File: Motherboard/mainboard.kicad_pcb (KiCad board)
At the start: 4 copper layers, 45.2 x 36 mm, 53 parts, among them IC1 BMX160, J1 Conn_01x01, J2 10118194-0001LF, J28 Conn_01x01, J29 Conn_01x01, J3 Micro_SD_Card, J30 Conn_01x01, J4 xf2m-2415-1a, J5 XF2M-1015-1A, J6 U.FL-R-SMT-1, J7 U.FL-R-SMT-1, J8 Conn_01x01, J9 XF2M36151A, SW1 KMR231NG LFS, U1 RFM95W-915S2, U2 ATSAMD51G_TQFN48, U3 DRV8848, U4 TPS82740BSIPR, U5 DRV8848, U6 MAX708RESA-T, U8 RFM95W-915S2

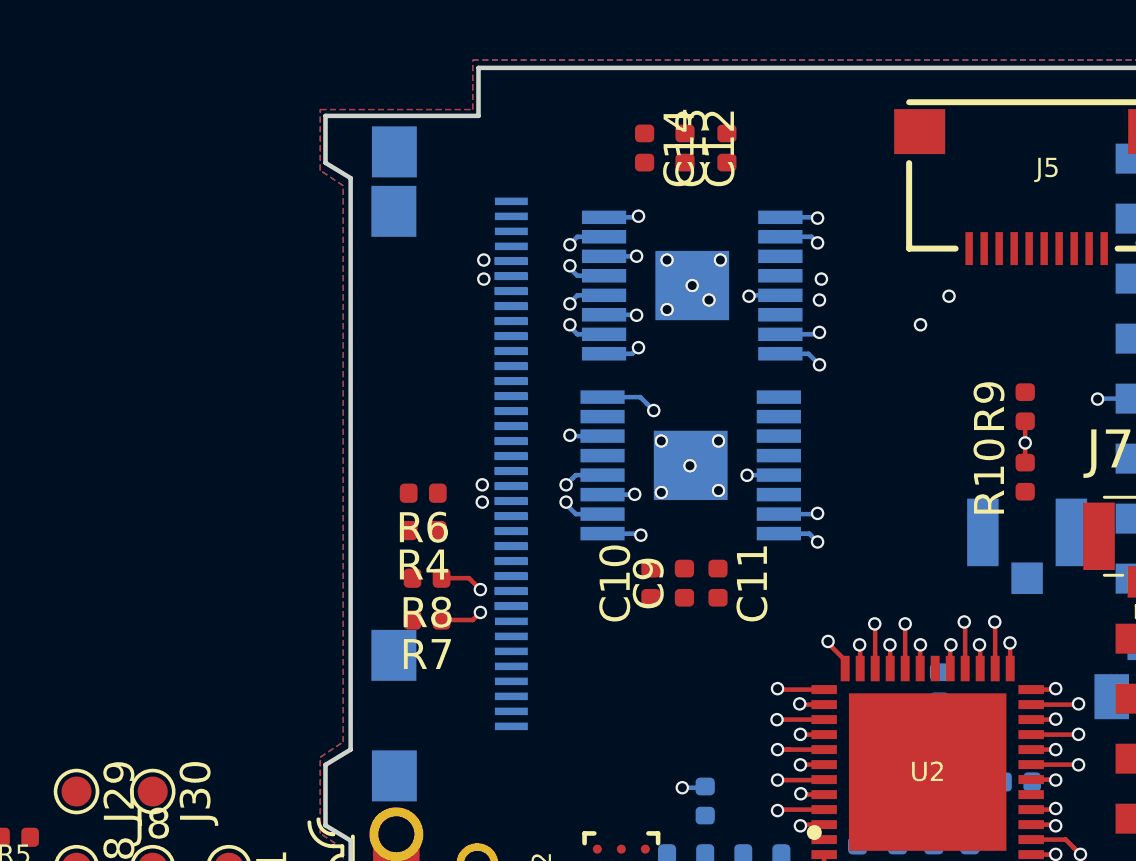
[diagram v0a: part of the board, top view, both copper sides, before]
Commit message: coil bridges with contingency finished
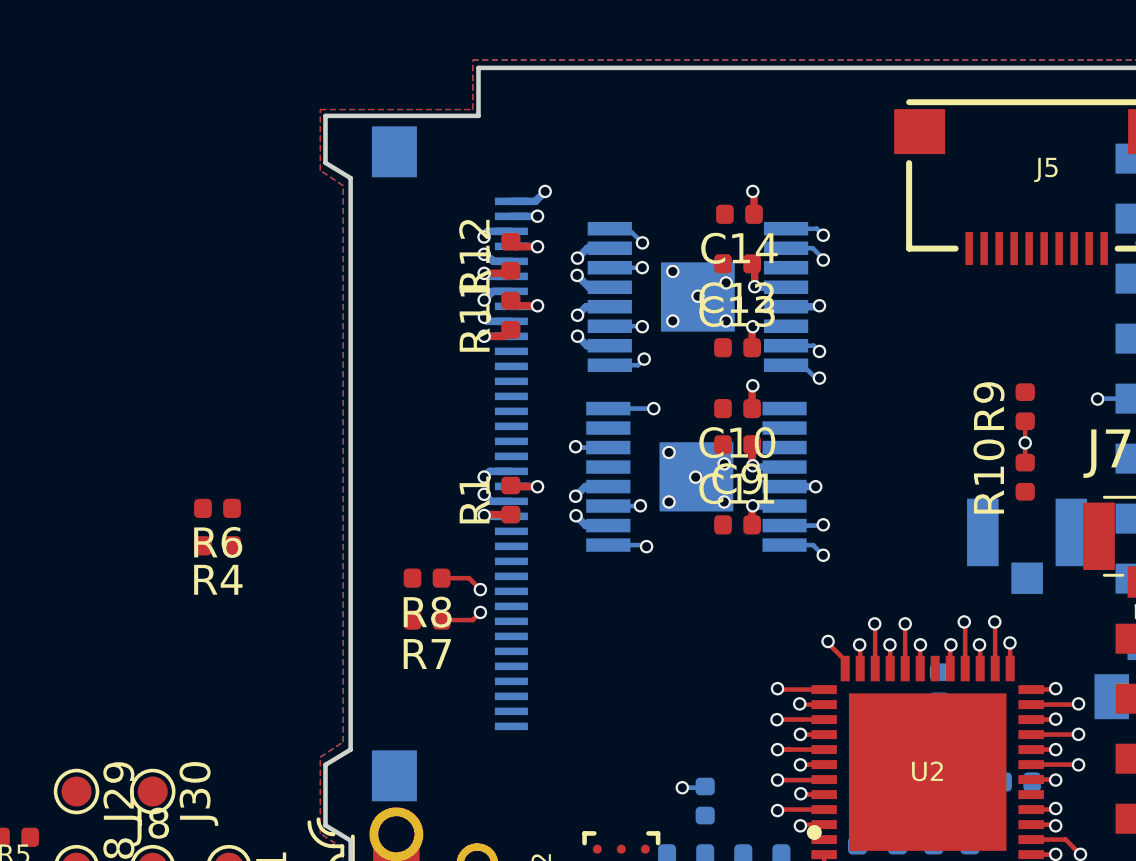
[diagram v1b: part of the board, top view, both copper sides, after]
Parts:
- removed J4: xf2m-2415-1a, custom-footprints:XF2M-2415-1A
- added R1: 0, Resistor_SMD:R_0402_1005Metric, F.Cu at (82.8, 87.9)
- added R11: 0, Resistor_SMD:R_0402_1005Metric, F.Cu at (82.8, 81.8)
- added R12: 0, Resistor_SMD:R_0402_1005Metric, F.Cu at (82.8, 79.8)
- moved R4 6.88 mm to (73.0, 89.5)
- moved R6 6.88 mm to (73.0, 88.2)
- moved C13 6.66 mm to (90.4, 82.9), turned to 0 degrees
- moved C10 6.50 mm to (90.4, 84.9), turned to 180 degrees
- moved C9 4.94 mm to (90.4, 86.1), turned to 180 degrees
- moved C12 4.24 mm to (90.4, 80.1), turned to 180 degrees
- moved C14 3.86 mm to (90.4, 78.4), turned to 180 degrees
- moved C11 2.05 mm to (90.4, 88.8), turned to 0 degrees
- moved U3 0.43 mm to (89.0, 81.2)
- moved U5 0.43 mm to (89.0, 87.2)
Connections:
- net Net-(J9-Pad16) renamed COIL6_N
- net Net-(J9-Pad18) renamed COIL5_P
- net Net-(J9-Pad28) renamed COIL4_N
- net Net-(J9-Pad30) renamed COIL3_P
- net Net-(J9-Pad32) renamed COIL2_N
- net Net-(J9-Pad34) renamed COIL1_P
- C11 pad 2: 3V3 -> +3V3
- C13 pad 2: 3V3 -> +3V3
- J9 pad 35: Net-(J9-Pad35) -> GND
- J9 pad 36: Net-(J9-Pad36) -> BATT_P
- U3 pad 11: 3V3 -> +3V3
- U3 pad 14: 3V3 -> +3V3
- U5 pad 11: 3V3 -> +3V3
- U5 pad 14: 3V3 -> +3V3
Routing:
- net BATT_P: track 0.00 -> 30.7 mm, vias 0 -> 5
- net (no net): track 30.2 -> 0.00 mm, vias 4 -> 0
- net MOX_1: track 4.55 -> 1.21 mm
- net MOX_2: track 4.49 -> 1.19 mm
- net MOY_1: track 4.45 -> 1.21 mm, vias 2 -> 1
- net MOZ_2: track 4.49 -> 1.25 mm, vias 2 -> 1
- net MOZ_1: track 4.34 -> 1.21 mm, vias 2 -> 1
- net MOY_2: track 4.25 -> 1.22 mm, vias 2 -> 1
- net MISO: track 59.1 -> 56.5 mm
- net +3V3: track 6.71 -> 9.25 mm, vias 8 -> 10
- net Net-(J9-Pad27): track 0.00 -> 1.89 mm, vias 0 -> 1
- net Net-(J9-Pad31): track 0.00 -> 1.87 mm, vias 0 -> 1
- net Net-(J9-Pad29): track 0.00 -> 1.84 mm, vias 0 -> 1
- net Net-(J9-Pad33): track 0.00 -> 1.83 mm, vias 0 -> 1
- net Net-(J9-Pad15): track 0.00 -> 1.82 mm, vias 0 -> 1
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
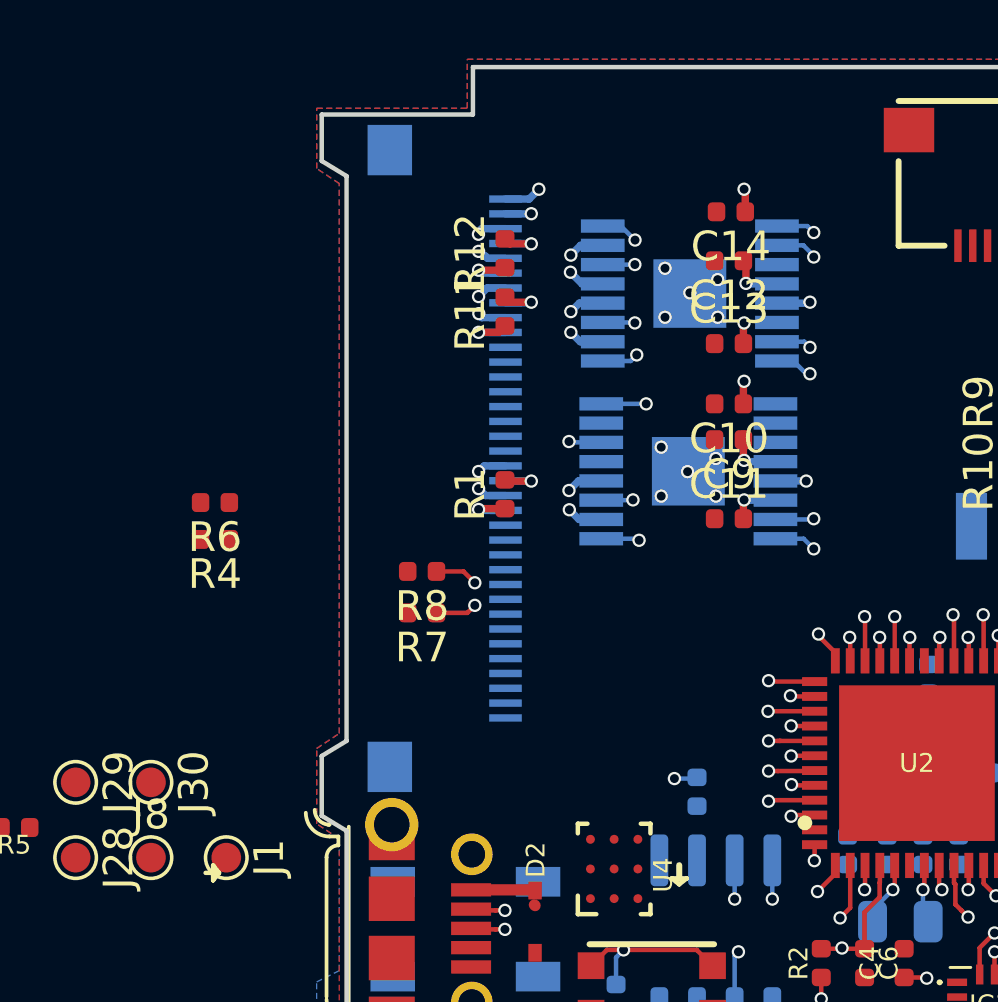
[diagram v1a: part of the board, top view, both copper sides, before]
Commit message: big FPC routed
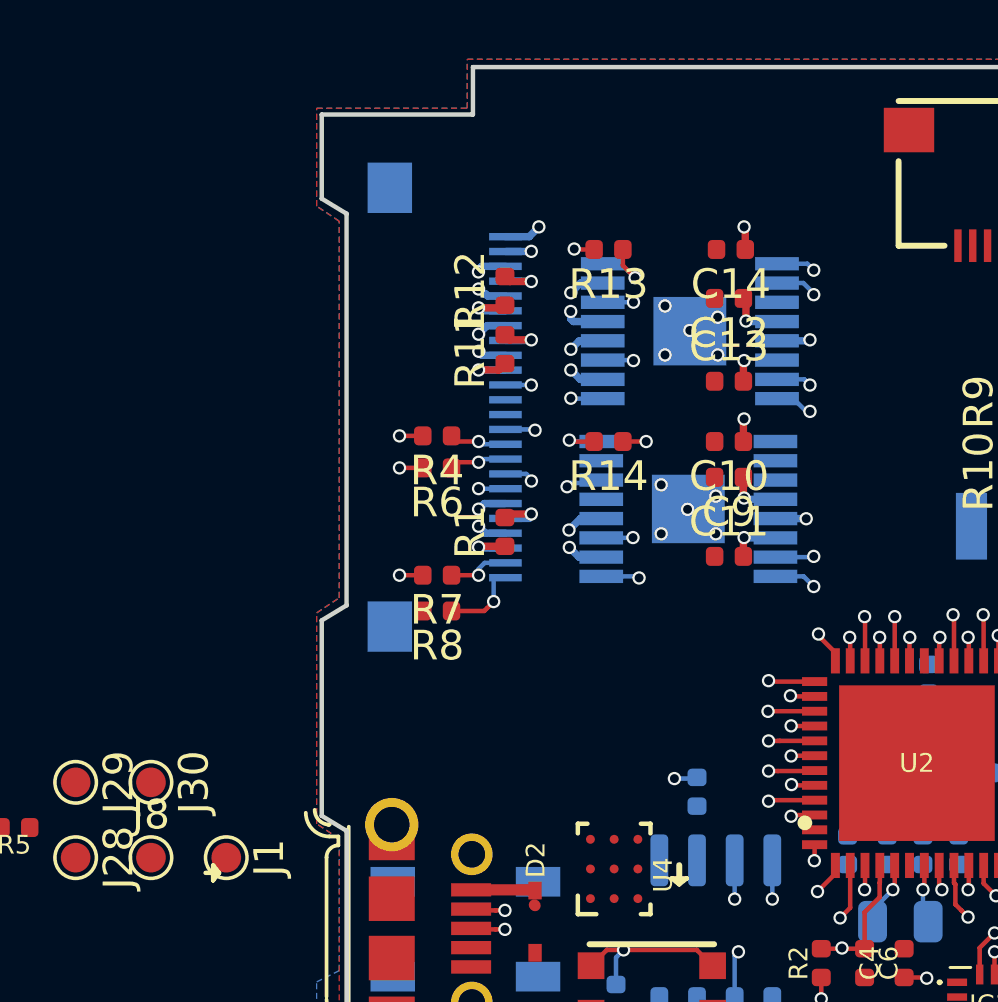
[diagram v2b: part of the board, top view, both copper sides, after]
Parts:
- removed J9: XF2M36151A, custom-footprints:XF2M36151A
- added J4: xf2m-2415-1a, custom-footprints:XF2M-2415-1A, B.Cu at (82.8, 85.0)
- added R13: 100K, Resistor_SMD:R_0402_1005Metric, F.Cu at (86.3, 79.7)
- added R14: 10K, Resistor_SMD:R_0402_1005Metric, F.Cu at (86.3, 86.2)
- moved R4 8.27 mm to (80.5, 86.0)
- moved R6 7.58 mm to (80.5, 87.1)
- moved R8 1.43 mm to (80.5, 91.9)
- moved R7 1.37 mm to (80.5, 90.7)
- moved C11 1.27 mm to (90.4, 90.0)
- moved C12 1.27 mm to (90.4, 81.3)
- moved C9 1.27 mm to (90.4, 87.4)
- moved R11 1.27 mm to (82.8, 83.1)
- moved U3 1.27 mm to (89.0, 82.4)
- moved U5 1.27 mm to (89.0, 88.4)
- moved C10 1.27 mm to (90.4, 86.2)
- moved C13 1.27 mm to (90.4, 84.1)
- moved C14 1.27 mm to (90.4, 79.7)
- moved R1 1.27 mm to (82.8, 89.2)
- moved R12 1.27 mm to (82.8, 81.1)
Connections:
- U3 pad 2: MOX_1 -> COIL4_N
- U3 pad 4: MOX_2 -> COIL3_P
- U3 pad 5: MOZ_2 -> COIL2_N
- U3 pad 7: MOZ_1 -> COIL1_P
- U5 pad 2: MOY_1 -> COIL6_N
- U5 pad 4: MOY_2 -> COIL5_P
- U5 pad 8: M_FAULT -> M_FAULT2
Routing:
- net SCL1: track 29.3 -> 34.9 mm, vias 2 -> 3
- net SDA1: track 27.2 -> 32.6 mm, vias 2 -> 3
- net COIL2_N: track 1.00 -> 5.79 mm, vias 1 -> 2
- net COIL1_P: track 1.03 -> 5.81 mm, vias 1 -> 2
- net COIL5_P: track 0.99 -> 5.73 mm, vias 1 -> 2
- net COIL3_P: track 1.03 -> 5.73 mm, vias 1 -> 2
- net COIL4_N: track 0.97 -> 5.55 mm, vias 1 -> 2
- net COIL6_N: track 1.00 -> 5.57 mm, vias 1 -> 2
- net BURN1: track 13.1 -> 17.1 mm, vias 1 -> 2
- net BATT_STATUS: track 12.8 -> 16.7 mm, vias 1 -> 2
- net BURN2: track 12.9 -> 16.4 mm, vias 1 -> 2
- net +3V3: track 9.25 -> 12.3 mm, vias 10 -> 14
- net M_FAULT2: track 0.00 -> 1.95 mm, vias 0 -> 1
- net SDA2: track 14.1 -> 15.8 mm
- net MINX_2: track 12.5 -> 11.3 mm
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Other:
- outline, holes or cut-outs redrawn

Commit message: neopixel 🚥
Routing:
- net RF2_BUSY: track 14.0 -> 11.5 mm
- net Net-(D3-Pad4): track 10.2 -> 11.8 mm, vias 1 -> 2
- net GND: track 11.7 -> 12.7 mm, vias 21 -> 22
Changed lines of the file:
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@@
     (thickness 1.2)
     (drawings 38)
-    (tracks 678)
+    (tracks 681)
     (zones 0)
     (modules 57)
@@
   )
   (setup
-    (last_trace_width 0.1524)
+    (last_trace_width 0.25)
     (user_trace_width 0.1524)
     (user_trace_width 0.25)
@@
   (segment (start 86.0509 87.4678) (end 85.9522 87.5665) (width 0.1524) (layer Bottom) (net 1))
   (segment (start 85.9522 87.5665) (end 85.026496 87.5665) (width 0.1524) (layer Bottom) (net 1))
+  (via (at 83.947 100.0125) (size 0.45) (drill 0.3) (layers Top Bottom) (net 1))
+  (segment (start 83.9205 101.016) (end 83.9205 100.039) (width 0.25) (layer Bottom) (net 1))
+  (segment (start 83.9205 100.039) (end 83.947 100.0125) (width 0.25) (layer Bottom) (net 1))
   (via (at 92.45601 98.806) (size 0.45) (drill 0.3) (layers Top Bottom) (net 2))
   (segment (start 93.2478 98.7653) (end 92.49671 98.7653) (width 0.1524) (layer Top) (net 2))
@@
   (segment (start 99.36375 101.489357) (end 99.697607 101.1555) (width 0.1524) (layer In1.Cu) (net 24))
   (segment (start 99.697607 101.1555) (end 114.173 101.1555) (width 0.1524) (layer In1.Cu) (net 24))
-  (via (at 105.3465 98.552) (size 0.45) (drill 0.3) (layers Top Bottom) (net 29))
-  (segment (start 103.86 98.568) (end 105.3305 98.568) (width 0.1524) (layer Top) (net 29))
-  (segment (start 105.3305 98.568) (end 105.3465 98.552) (width 0.1524) (layer Top) (net 29))
   (via (at 94.9325 101.2825) (size 0.45) (drill 0.3) (layers Top Bottom) (net 29))
   (segment (start 94.9478 100.4653) (end 94.9478 101.2672) (width 0.1524) (layer Top) (net 29))
   (segment (start 94.9478 101.2672) (end 94.9325 101.2825) (width 0.1524) (layer Top) (net 29))
-  (segment (start 104.013 98.552) (end 105.3465 98.552) (width 0.1524) (layer In1.Cu) (net 29))
-  (segment (start 98.7425 100.711) (end 99.314 100.1395) (width 0.1524) (layer In1.Cu) (net 29))
-  (segment (start 95.504 100.711) (end 98.7425 100.711) (width 0.1524) (layer In1.Cu) (net 29))
-  (segment (start 99.314 100.1395) (end 100.584 100.1395) (width 0.1524) (layer In1.Cu) (net 29))
-  (segment (start 102.235 100.33) (end 104.013 98.552) (width 0.1524) (layer In1.Cu) (net 29))
-  (segment (start 94.9325 101.2825) (end 95.504 100.711) (width 0.1524) (layer In1.Cu) (net 29))
-  (segment (start 100.584 100.1395) (end 100.7745 100.33) (width 0.1524) (layer In1.Cu) (net 29))
-  (segment (start 100.7745 100.33) (end 102.235 100.33) (width 0.1524) (layer In1.Cu) (net 29))
   (via (at 101.727008 96.774) (size 0.45) (drill 0.3) (layers Top Bottom) (net 31))
   (segment (start 101.718308 96.7653) (end 101.727008 96.774) (width 0.1524) (layer Top) (net 31))
@@
   (segment (start 119.66 96.568) (end 118.189 96.568) (width 0.1524) (layer Top) (net 31))
   (segment (start 118.189 96.568) (end 118.1735 96.5835) (width 0.1524) (layer Top) (net 31))
-  (segment (start 102.9208 96.774) (end 101.727008 96.774) (width 0.1524) (layer In1.Cu) (net 31))
-  (segment (start 118.1735 96.5835) (end 103.1113 96.5835) (width 0.1524) (layer In1.Cu) (net 31))
-  (segment (start 103.1113 96.5835) (end 102.9208 96.774) (width 0.1524) (layer In1.Cu) (net 31))
   (segment (start 88.011 105.445) (end 89.281 105.445) (width 0.1524) (layer Bottom) (net 32))
   (segment (start 88.0055 105.4505) (end 88.011 105.445) (width 0.1524) (layer Bottom) (net 32))
@@
   (segment (start 119.66 86.566) (end 119.66 87.4135) (width 0.1524) (layer Bottom) (net 69))
   (segment (start 119.66 87.4135) (end 119.634 87.4395) (width 0.1524) (layer Bottom) (net 69))
-  (segment (start 103.124 96.266) (end 100.965 96.266) (width 0.1524) (layer In1.Cu) (net 69))
-  (segment (start 103.55834 95.83166) (end 103.124 96.266) (width 0.1524) (layer In1.Cu) (net 69))
-  (segment (start 119.634 87.4395) (end 111.24184 95.83166) (width 0.1524) (layer In1.Cu) (net 69))
-  (segment (start 111.24184 95.83166) (end 103.55834 95.83166) (width 0.1524) (layer In1.Cu) (net 69))
   (via (at 101.727 95.758) (size 0.45) (drill 0.3) (layers Top Bottom) (net 70))
   (segment (start 100.1478 95.7653) (end 101.7197 95.7653) (width 0.1524) (layer Top) (net 70))
@@
   (segment (start 93.345 101.3431) (end 93.345 101.34601) (width 0.1524) (layer Top) (net 77))
   (segment (start 93.9478 100.4653) (end 93.9478 100.7403) (width 0.1524) (layer Top) (net 77))
-  (segment (start 92.2655 102.4255) (end 84.7725 102.4255) (width 0.1524) (layer In1.Cu) (net 77))
-  (segment (start 93.345 101.34601) (end 93.34499 101.34601) (width 0.1524) (layer In1.Cu) (net 77))
-  (segment (start 93.34499 101.34601) (end 92.2655 102.4255) (width 0.1524) (layer In1.Cu) (net 77))
   (via (at 83.693 80.772) (size 0.45) (drill 0.3) (layers Top Bottom) (net 86))
   (segment (start 82.822 80.761) (end 83.682 80.761) (width 0.25) (layer Bottom) (net 86))
@@
   (segment (start 82.9715 82.7405) (end 82.804 82.573) (width 0.25) (layer Top) (net 26))
   (segment (start 83.693 82.7405) (end 82.9715 82.7405) (width 0.25) (layer Top) (net 26))
+  (via (at 103.886 99.377496) (size 0.45) (drill 0.3) (layers Top Bottom) (net 29))
+  (segment (start 102.933496 100.33) (end 103.661001 99.602495) (width 0.1524) (layer In1.Cu) (net 29))
+  (segment (start 103.86 98.568) (end 103.86 99.351496) (width 0.1524) (layer Top) (net 29))
+  (segment (start 100.7745 100.33) (end 102.933496 100.33) (width 0.1524) (layer In1.Cu) (net 29))
+  (segment (start 103.661001 99.602495) (end 103.886 99.377496) (width 0.1524) (layer In1.Cu) (net 29))
+  (segment (start 100.584 100.1395) (end 100.7745 100.33) (width 0.1524) (layer In1.Cu) (net 29))
+  (segment (start 96.0755 100.1395) (end 100.584 100.1395) (width 0.1524) (layer In1.Cu) (net 29))
+  (segment (start 94.9325 101.2825) (end 96.0755 100.1395) (width 0.1524) (layer In1.Cu) (net 29))
+  (segment (start 103.86 99.351496) (end 103.886 99.377496) (width 0.1524) (layer Top) (net 29))
+  (segment (start 102.9208 96.774) (end 101.727008 96.774) (width 0.1524) (layer In1.Cu) (net 31))
+  (segment (start 118.1735 96.5835) (end 117.983 96.774) (width 0.1524) (layer In1.Cu) (net 31))
+  (segment (start 117.983 96.774) (end 102.9208 96.774) (width 0.1524) (layer In1.Cu) (net 31))
   (via (at 81.915 90.678) (size 0.45) (drill 0.3) (layers Top Bottom) (net 39))
   (segment (start 82.82178 90.26126) (end 82.11938 90.26126) (width 0.1524) (layer Bottom) (net 39))
@@
   (segment (start 82.92301 88.61349) (end 83.693 88.61349) (width 0.25) (layer Top) (net 51))
   (segment (start 82.804 88.7325) (end 82.92301 88.61349) (width 0.25) (layer Top) (net 51))
+  (segment (start 110.8075 96.266) (end 100.965 96.266) (width 0.1524) (layer In1.Cu) (net 69))
+  (segment (start 119.634 87.4395) (end 110.8075 96.266) (width 0.1524) (layer In1.Cu) (net 69))
   (via (at 83.82 85.7885) (size 0.45) (drill 0.3) (layers Top Bottom) (net 72))
   (segment (start 82.82178 85.76126) (end 83.79276 85.76126) (width 0.1524) (layer Bottom) (net 72))
@@
   (segment (start 85.513609 88.955309) (end 85.513609 85.196105) (width 0.1524) (layer In2.Cu) (net 74))
   (segment (start 85.513609 85.196105) (end 85.251503 84.933999) (width 0.1524) (layer In2.Cu) (net 74))
+  (via (at 84.6455 103.378) (size 0.45) (drill 0.3) (layers Top Bottom) (net 77))
+  (segment (start 83.9205 104.216) (end 83.9205 104.103) (width 0.1524) (layer Bottom) (net 77))
+  (segment (start 83.9205 104.103) (end 84.6455 103.378) (width 0.1524) (layer Bottom) (net 77))
+  (segment (start 85.598 102.4255) (end 84.6455 103.378) (width 0.1524) (layer In1.Cu) (net 77))
+  (segment (start 92.2655 102.4255) (end 85.598 102.4255) (width 0.1524) (layer In1.Cu) (net 77))
+  (segment (start 93.345 101.34601) (end 93.34499 101.34601) (width 0.1524) (layer In1.Cu) (net 77))
+  (segment (start 93.34499 101.34601) (end 92.2655 102.4255) (width 0.1524) (layer In1.Cu) (net 77))
   (segment (start 81.944987 89.761) (end 81.915 89.731013) (width 0.25) (layer Bottom) (net 78))
   (segment (start 82.822 89.761) (end 81.944987 89.761) (width 0.25) (layer Bottom) (net 78))

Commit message: 100% routed
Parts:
- removed J28, J29, J30, J8: Conn_01x01, TestPoint:TestPoint_Pad_D1.0mm
- added J9: Conn_01x02, Connector_PinHeader_2.54mm:PinHeader_1x02_P2.54mm_Vertical, F.Cu at (90.0, 77.0)
- J1: value Conn_01x01 -> Conn_01x06; footprint TestPoint:TestPoint_Pad_D1.0mm -> Connector_PinHeader_1.27mm:PinHeader_2x03_P1.27mm_Vertical_SMD
- moved R5 22.2 mm to (88.1, 95.4), turned to 180 degrees
- moved J1 10.6 mm to (82.9, 95.4), turned to 0 degrees
- moved J5 1.49 mm to (99.8, 81.0)
- moved C16 0.63 mm to (88.8, 98.4), turned to 180 degrees
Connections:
- J1 pad 1: /SWDIO -> +3V3
- J3 pad SH1: (no net) -> GND
- J5 pad 4: BATT_N -> GND
- J5 pad 5: EN_CAM -> MOSI
- J5 pad 6: CS_CAM -> SCK
- J5 pad 8: MOSI -> EN_CAM
- J5 pad 9: SCK -> CS_CAM
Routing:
- net BATT_P: track 30.7 -> 44.9 mm, vias 5 -> 7
- net /SWCLK: track 7.63 -> 20.0 mm, vias 1 -> 2
- net /SWDIO: track 6.02 -> 17.7 mm, vias 1 -> 2
- net ~RESET: track 18.4 -> 28.5 mm, vias 2 -> 3
- net MISO: track 56.5 -> 66.5 mm, vias 4 -> 5
- net /USB+: track 4.56 -> 12.9 mm
- net /USB-: track 5.13 -> 13.3 mm
- net CS_CAM: track 10.4 -> 15.5 mm, vias 1 -> 2
- net GND: track 12.7 -> 16.1 mm, vias 22 -> 24
- net EN_CAM: track 10.5 -> 12.9 mm, vias 1 -> 2
- net MOSI: track 57.1 -> 58.9 mm, vias 4 -> 5
- net +3V3: track 12.3 -> 13.9 mm, vias 14 -> 15
- net SCK: track 55.1 -> 55.5 mm, vias 4 -> 5

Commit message: finished- might fiddle with later
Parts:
- moved D2 2.03 mm to (83.8, 100.3), turned to 270 degrees
- moved R5 1.88 mm to (87.2, 97.1), turned to 90 degrees
- renumbered IC1 to U7
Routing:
- net GND: track 16.1 -> 29.9 mm, vias 24 -> 38
- net Net-(D2-Pad1): track 0.00 -> 5.59 mm
- net +3V3: track 13.9 -> 18.5 mm, vias 15 -> 21
- net Net-(J6-Pad3): track 0.00 -> 3.85 mm
- net Net-(J7-Pad3): track 0.00 -> 1.86 mm
- net ~RESET: track 28.5 -> 29.9 mm
- net MINY_2: track 11.9 -> 10.6 mm
- net MINY_1: track 5.51 -> 4.24 mm
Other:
- board text added: "BATTP"
- board text added: "RADIO #1"
- board text added: "RADIO #2"
- board text added: "RST"
- board text added: "~RESET"

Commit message: fab files for max version of MB
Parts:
- added Ref**: Val**, custom-footprints:XYZ_mini, F.Cu at (110.0, 81.3)
- added Ref**: Val**, custom-footprints:holliday, B.Cu at (76.3, 94.8)
- added Ref**: Val**, custom-footprints:version, B.Cu at (93.9, 105.6)
- added Ref**: Val**, custom-footprints:version, F.Cu at (78.7, 86.2)
- added Ref**: Val**, custom-footprints:pycubed_mini_logo, B.Cu at (97.5, 76.0)
- added Ref**: Val**, custom-footprints:pycubed_mini_logo, F.Cu at (117.5, 83.9)
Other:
- board text added: "C+M"
